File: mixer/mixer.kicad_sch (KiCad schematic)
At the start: 16 parts, among them J4 Conn_Coaxial, J5 Conn_Coaxial, J6 AudioJack3, J7 AudioJack3, P1 PMOD-Device-x2-Type-Generic-A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, U17 TLE4284 DV33, U3 Si5351C-B-GU, U5 uA7805, X8 TCXO-14

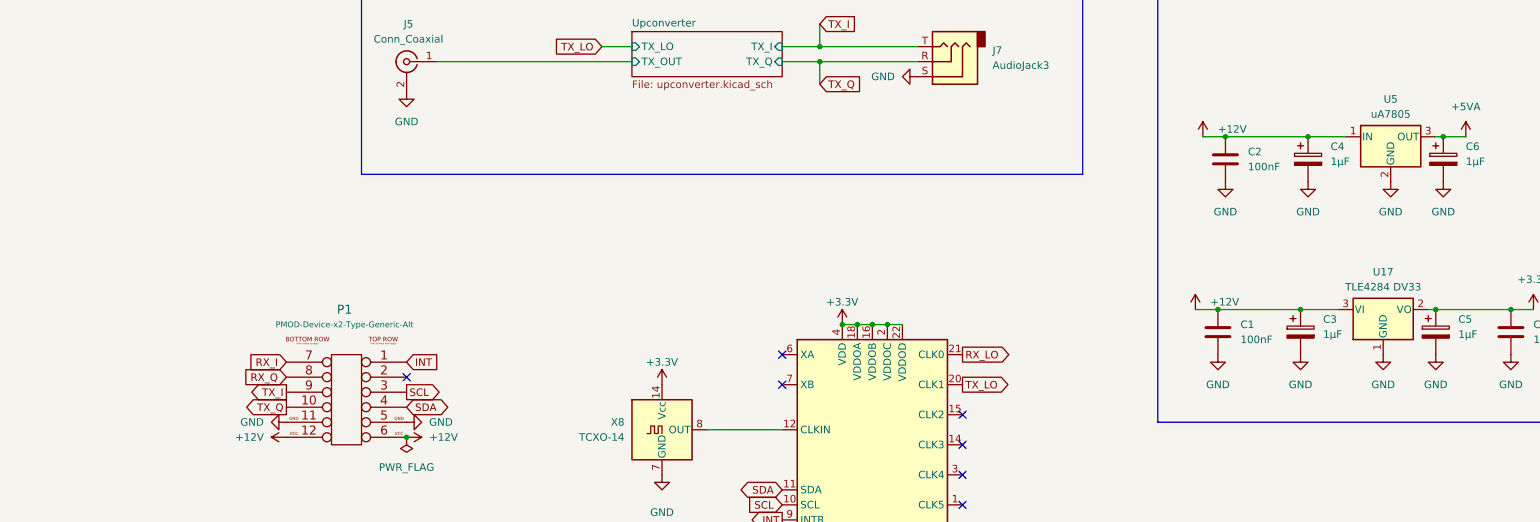
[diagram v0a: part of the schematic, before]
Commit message: use lt1117 as linear voltage regulator
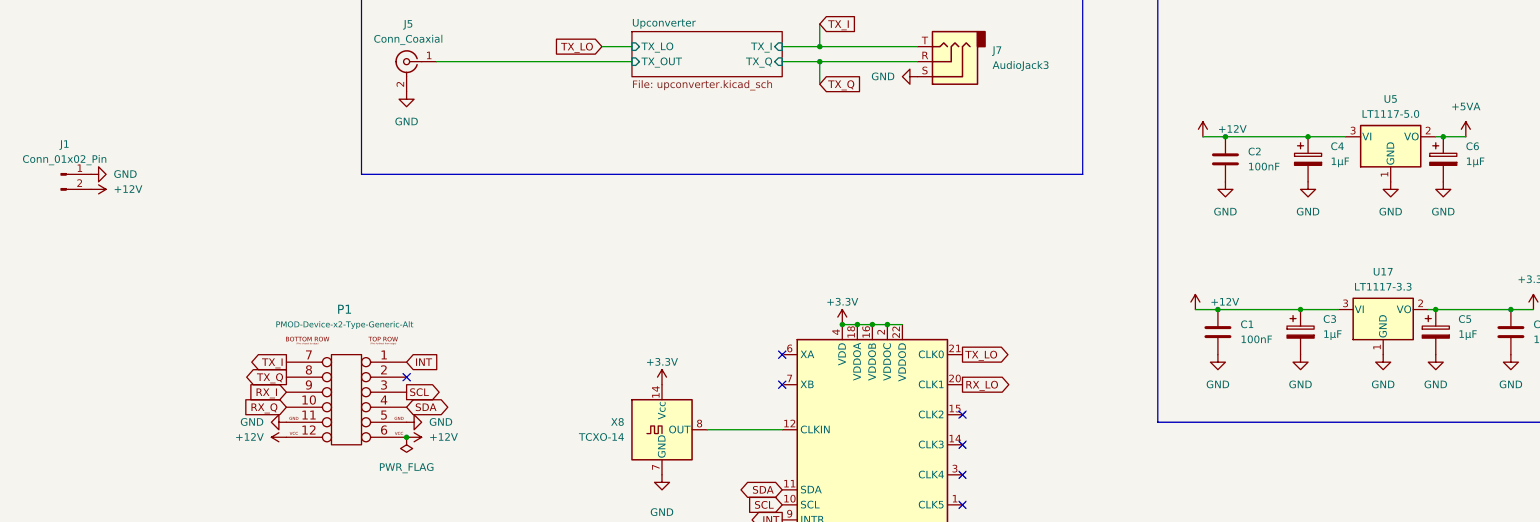
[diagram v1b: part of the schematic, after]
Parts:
- removed U17: TLE4284 DV33, Package_TO_SOT_SMD:TO-252-3_TabPin2, symbol Regulator_Linear:AMS1117CD-3.3
- removed U5: uA7805, Package_TO_SOT_THT:TO-220-3_Vertical, symbol Regulator_Linear:uA7805
- added J1: Conn_01x02_Pin, Connector_JST:JST_VH_S2P-VH_1x02_P3.96mm_Horizontal, symbol Connector:Conn_01x02_Pin
- added U17: LT1117-3.3, Package_TO_SOT_SMD:SOT-223-3_TabPin2, symbol Regulator_Linear:LT1117-3.3
- added U5: LT1117-5.0, Package_TO_SOT_SMD:SOT-223-3_TabPin2, symbol Regulator_Linear:LT1117-5.0
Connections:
- net +12V: now also J1.2 (Pin_2), U17.3 (VI), U5.3 (VI)
- net +3.3V: now also U17.2 (VO)
- net +5VA: now also U5.2 (VO)
- net GND: now also J1.1 (Pin_1), U17.1 (GND), U5.1 (GND)
- net RX_I: now also P1.9 (P9); no longer P1.7 (P7)
- net RX_LO: now also U3.20 (CLK1); no longer U3.21 (CLK0)
- net RX_Q: now also P1.10 (P10); no longer P1.8 (P8)
- net TX_I: now also P1.7 (P7); no longer P1.9 (P9)
- net TX_LO: now also U3.21 (CLK0); no longer U3.20 (CLK1)
- net TX_Q: now also P1.8 (P8); no longer P1.10 (P10)

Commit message: replace RF connectors, add missing silkscreen text
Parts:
- J4, J5: footprint Connector_Coaxial:SMA_Amphenol_132291_Vertical -> Connector_Coaxial:SMA_Molex_73251-2200_Horizontal
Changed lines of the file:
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@@
 			)
 		)
-		(property "Footprint" "Connector_Coaxial:SMA_Amphenol_132291_Vertical"
+		(property "Footprint" "Connector_Coaxial:SMA_Molex_73251-2200_Horizontal"
 			(at 63.5 76.2 0)
 			(effects
@@
 			)
 		)
-		(property "Footprint" "Connector_Coaxial:SMA_Amphenol_132291_Vertical"
+		(property "Footprint" "Connector_Coaxial:SMA_Molex_73251-2200_Horizontal"
 			(at 21.59 38.1 0)
 			(effects

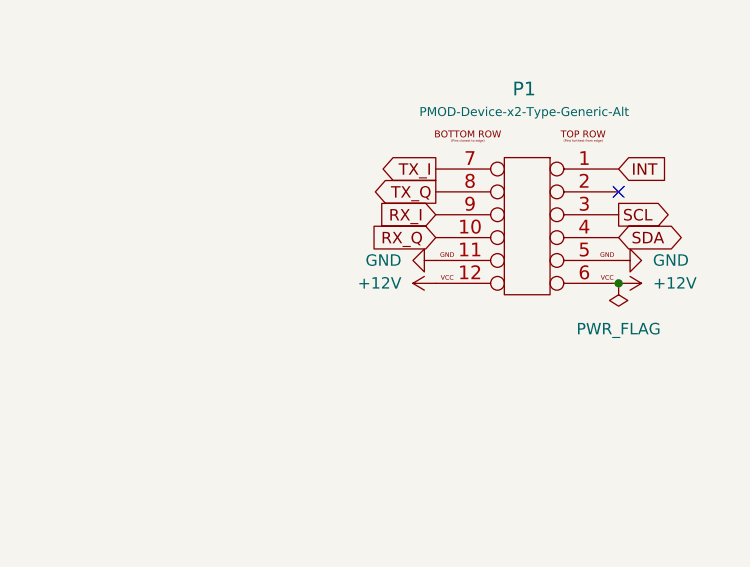
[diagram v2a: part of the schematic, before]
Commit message: add gerber export settings and get drc-clean
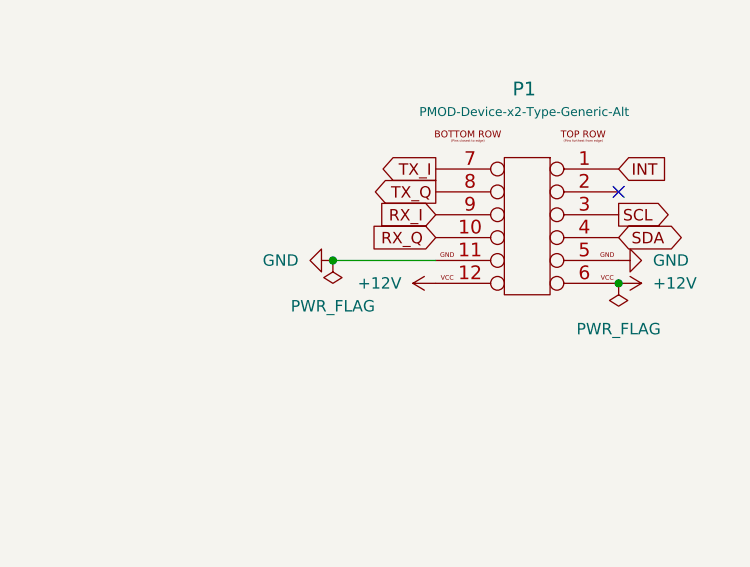
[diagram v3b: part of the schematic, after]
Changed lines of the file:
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@@
 	)
 	(junction
+		(at 31.75 137.16)
+		(diameter 0)
+		(color 0 0 0 0)
+	)
+	(junction
 		(at 137.16 120.65)
 		(diameter 0)
@@
 	(wire
 		(pts
+			(xy 31.75 137.16) (xy 43.18 137.16)
+		)
+		(stroke
+			(width 0)
+			(type default)
+		)
+	)
+	(wire
+		(pts
 			(xy 133.35 76.2) (xy 133.35 80.01)
 		)
@@
 			)
 		)
-		(property "Datasheet" " ~"
+		(property "Datasheet" "~"
 			(at 63.5 76.2 0)
 			(effects
@@
 	(symbol
 		(lib_id "power:GND")
-		(at 43.18 137.16 270)
+		(at 31.75 137.16 270)
 		(unit 1)
 		(exclude_from_sim no)
@@
 		(fields_autoplaced yes)
 		(property "Reference" "#PWR04"
-			(at 36.83 137.16 0)
+			(at 25.4 137.16 0)
 			(effects
 				(font
@@
 		)
 		(property "Value" "GND"
-			(at 39.37 137.1599 90)
+			(at 27.94 137.1599 90)
 			(effects
 				(font
@@
 		)
 		(property "Footprint" ""
-			(at 43.18 137.16 0)
+			(at 31.75 137.16 0)
 			(effects
 				(font
@@
 		)
 		(property "Datasheet" ""
-			(at 43.18 137.16 0)
+			(at 31.75 137.16 0)
 			(effects
 				(font
@@
 		)
 		(property "Description" "Power symbol creates a global label with name \"GND\" , ground"
-			(at 43.18 137.16 0)
+			(at 31.75 137.16 0)
 			(effects
 				(font
@@
 			)
 		)
-		(property "Datasheet" " ~"
+		(property "Datasheet" "~"
 			(at 21.59 38.1 0)
 			(effects
@@
 					(unit 1)
 				)
+			)
+		)
+	)
+	(symbol
+		(lib_id "power:PWR_FLAG")
+		(at 31.75 137.16 180)
+		(unit 1)
+		(exclude_from_sim no)
+		(in_bom yes)
+		(on_board yes)
+		(dnp no)
+		(fields_autoplaced yes)
+		(property "Reference" "#FLG01"
+			(at 31.75 139.065 0)
+			(effects
+				(font
+					(size 1.27 1.27)
+				)
+				(hide yes)
+			)
+		)
+		(property "Value" "PWR_FLAG"
+			(at 31.75 142.24 0)
+			(effects
+				(font
+					(size 1.27 1.27)
+				)
+			)
+		)
+		(property "Footprint" ""
+			(at 31.75 137.16 0)
+			(effects
+				(font
+					(size 1.27 1.27)
+				)
+				(hide yes)
+			)
+		)
+		(property "Datasheet" "~"
+			(at 31.75 137.16 0)
+			(effects
+				(font
+					(size 1.27 1.27)
+				)
+				(hide yes)
+			)
+		)
+		(property "Description" "Special symbol for telling ERC where power comes from"
+			(at 31.75 137.16 0)
+			(effects
+				(font
+					(size 1.27 1.27)
+				)
+				(hide yes)
+			)
+		)
+		(pin "1"
+		)
+		(instances
+			(project "mixer"
+				(path "/baafbbfa-2a96-4840-9dde-bc29ad2a66a8"
+					(reference "#FLG01")
+					(unit 1)
+				)
